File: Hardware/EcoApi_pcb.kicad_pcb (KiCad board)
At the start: 4 copper layers, 90.6 x 58 mm, 171 parts, among them IC1 PCF8563T_5,518, IC2 SIP32431DR3-T1GE3, IC3 SIP32431DR3-T1GE3, J1 UFL, J10 TILT, J12 POWER ON, J2 614105150721, J3 B2B-XH-A, J4 POWER ON, J5 Debug, J7 I2C INTERNAL, J8 B5B-XH-A__LF__SN_, J9 B8B-XH-A_LF__SN_, Q1 MMBT4403, Q2 FDC638P, Q3 IRLML6244TRPBF, Q4 BSS138, Q5 BSS138, Q6 IRLML6244TRPBF, Q7 FDC638P, Q8 BSS84AK,215, Q9 BSS84AK,215, U1 TPL5010DDCR, U10 TPS63900DSKR, U13 STM32F411CEU6, U2 HX711, U4 MB85RC04VPNF-G-JNERE1, U5 RFM95W-868S2, U6 W25Q32JVSS, U7 24LC02BT-I/SN, U8 TP4056M, Y1 32.768kHz 12.5pF, Y2 32.768kHz 6pF, Y3 25mHz 9pF +-10ppm

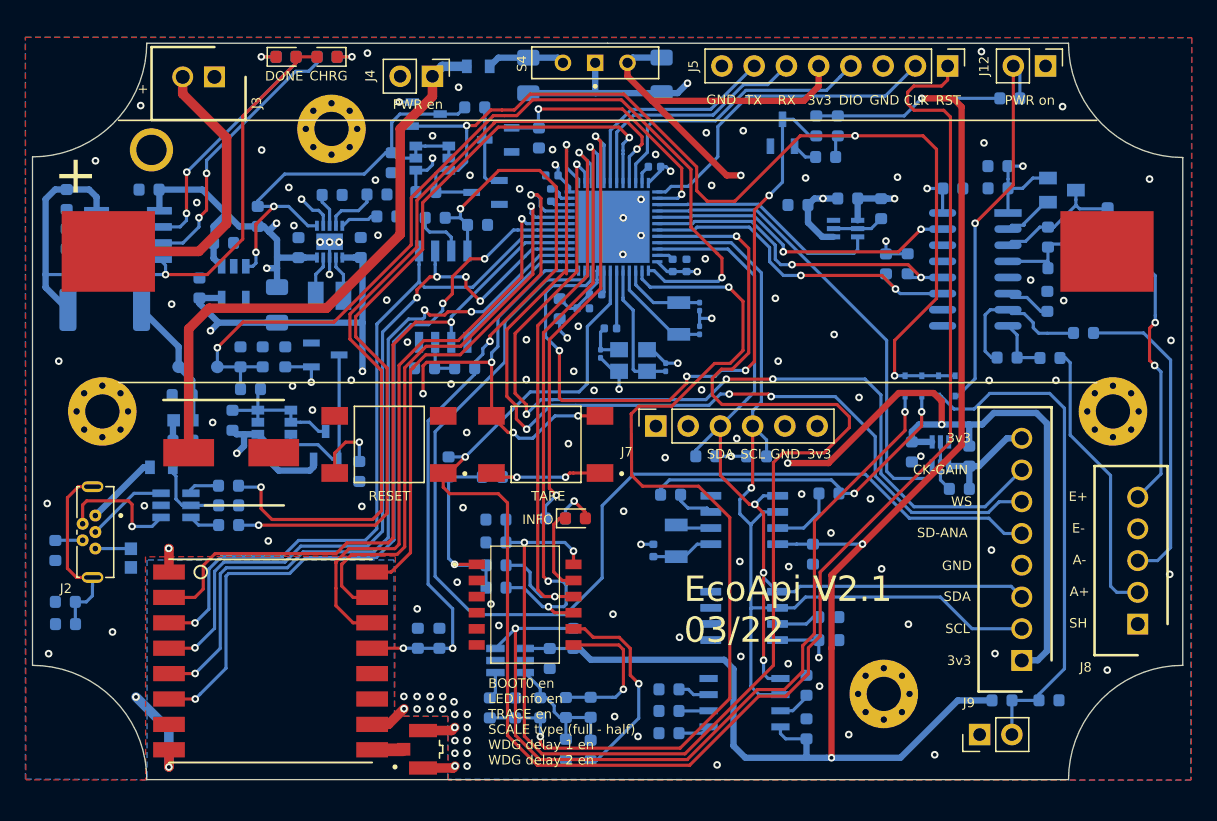
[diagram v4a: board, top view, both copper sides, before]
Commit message: Fix JLCPCB assembly issues, Add reverse battery protection, Define Correct crystal capa, Add Layer number and fiducial, and some quicq fix
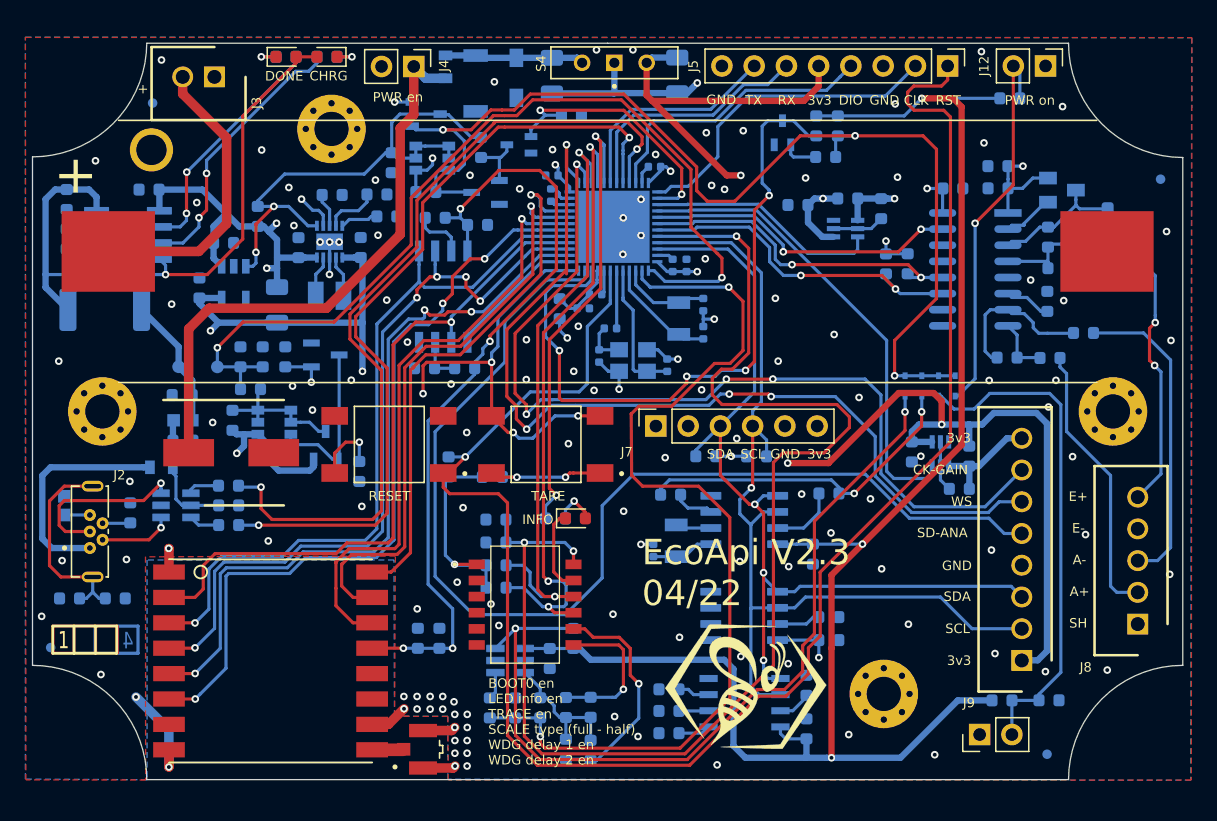
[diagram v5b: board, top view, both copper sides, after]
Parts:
- added D10: PMEG10020AELPX, EcoApi_pcb:SODFL4725X110N, B.Cu at (173.9, 41.2)
- added D9: PMEG10010ELRX, EcoApi_pcb:SOD123_Generic(W_F_FL), B.Cu at (177.1, 40.7)
- added G***: LOGO, EcoApi_pcb:Logo_EcoApi, F.Cu at (195.2, 88.7)
- added LayerIcon04: VAL**, EcoApi_pcb:LayerNumber_4, F.Cu at (143.6, 85.0)
- added REF**: Fiducial_0.75mm_Mask1.5mm, Fiducial:Fiducial_0.75mm_Mask1.5mm, B.Cu at (218.9, 94.0)
- added REF**: Fiducial_0.75mm_Mask1.5mm, Fiducial:Fiducial_0.75mm_Mask1.5mm, B.Cu at (227.8, 48.7)
- added REF**: Fiducial_0.75mm_Mask1.5mm, Fiducial:Fiducial_0.75mm_Mask1.5mm, B.Cu at (140.4, 85.6)
- added REF**: Fiducial_0.75mm_Mask1.5mm, Fiducial:Fiducial_0.75mm_Mask1.5mm, B.Cu at (148.5, 42.7)
- C33, C34, C35, C36: footprint Capacitor_SMD:C_0201_0603Metric -> Capacitor_SMD:C_0402_1005Metric
- Q4, Q5: footprint EcoApi_pcb:SOT95P240X111-3N -> EcoApi_pcb:SOT65P210X110-3N
- R36, R37: value 330R -> 1K
- R72: value 1.5K -> 1K
- U8: value TP4056M -> TP4056X
- moved FB1 6.68 mm to (141.5, 74.4), turned to 90 degrees
- moved R38 6.60 mm to (146.7, 75.0), turned to 90 degrees
- moved C17 4.41 mm to (145.5, 81.7), turned to 0 degrees
- moved R48 3.20 mm to (174.3, 46.2), turned to 270 degrees
- moved R50 3.12 mm to (181.4, 43.7), turned to 0 degrees
- moved F2 2.58 mm to (171.5, 39.9), turned to 90 degrees
- moved R46 1.86 mm to (179.9, 40.5)
- moved Q4 1.68 mm to (177.3, 46.0)
- moved J4 1.66 mm to (169.0, 39.8)
- moved S4 1.51 mm to (184.8, 39.5)
- moved R56 1.23 mm to (189.8, 40.5)
- moved J2 0.43 mm to (143.5, 76.5), turned to 90 degrees
- moved R34 0.43 mm to (141.9, 81.7)
- moved C34 0.35 mm to (191.8, 60.8)
- moved C33 0.33 mm to (191.8, 58.6)
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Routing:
- net Net-(F1-Pad1): track 5.87 -> 17.8 mm
- net Net-(D8-Pad3): track 6.44 -> 13.8 mm, vias 0 -> 1
- net VBATT: track 51.0 -> 56.1 mm
- net Net-(D8-Pad1): track 9.95 -> 5.81 mm
- net Net-(Q3-Pad1): track 6.77 -> 4.57 mm
- net EN_3V3: track 39.0 -> 40.8 mm
- net Net-(C17-Pad1): track 14.9 -> 16.4 mm
- net Net-(BT1-Pad+): track 43.5 -> 42.4 mm
- net V_WKUP: track 146.0 -> 144.9 mm
- net WAKEUP: track 53.8 -> 54.7 mm
- net PWR_ON: track 86.8 -> 87.7 mm
- net Net-(Q5-Pad1): track 2.01 -> 2.80 mm
- net Net-(FB1-Pad1): track 2.81 -> 2.02 mm
- net +3V3: track 145.7 -> 145.2 mm
- net GND: track 44.7 -> 44.5 mm, vias 120 -> 127
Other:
- board text added: "EcoApi V2.3 04/22"
- board text removed: "EcoApi V2.1 03/22"
